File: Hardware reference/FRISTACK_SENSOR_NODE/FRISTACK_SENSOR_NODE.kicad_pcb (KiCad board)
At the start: 2 copper layers, 30 x 55 mm, 68 parts, among them J1 SPI_Header, J2 I2C/GPIO/I2S, J3 BATT, U1 ESP32-H2-MINI-1, Y1 32.768 kHz

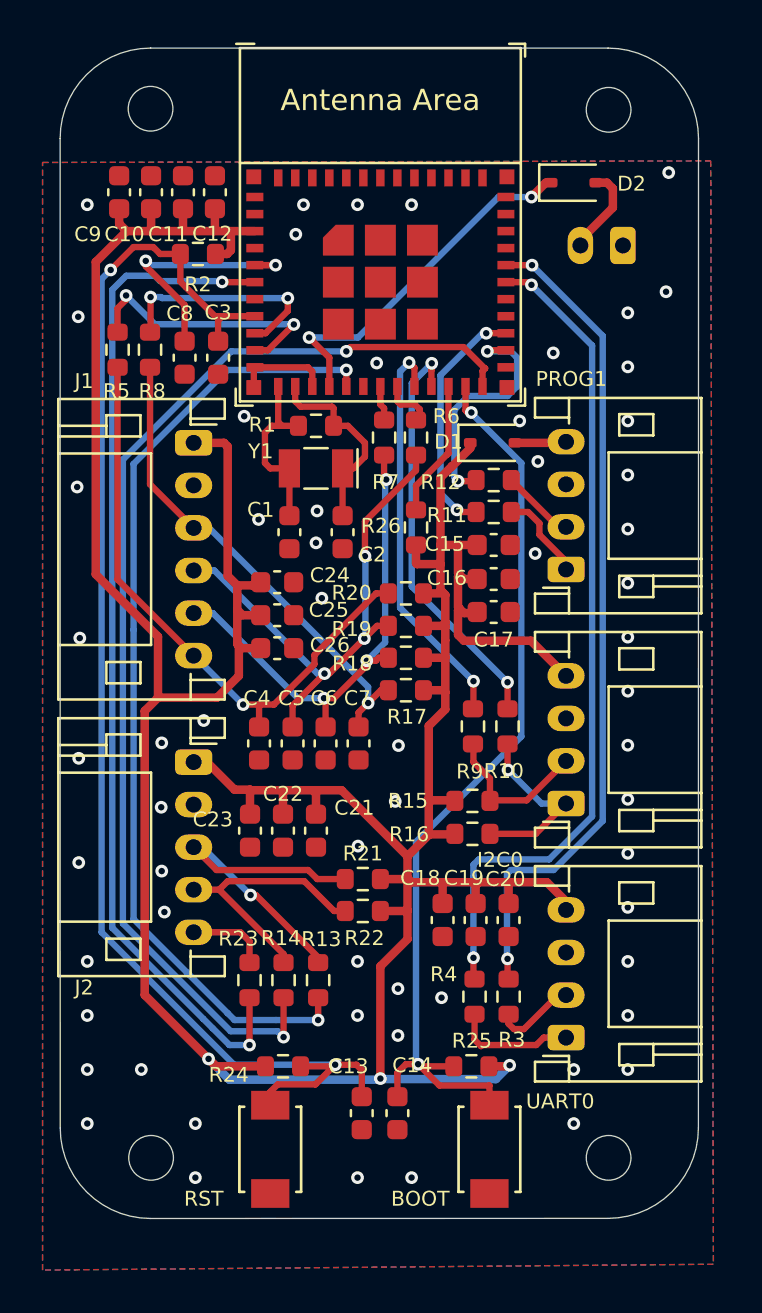
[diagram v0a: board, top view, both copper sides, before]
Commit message: Power management changes on CORE and SENSOR_NODE
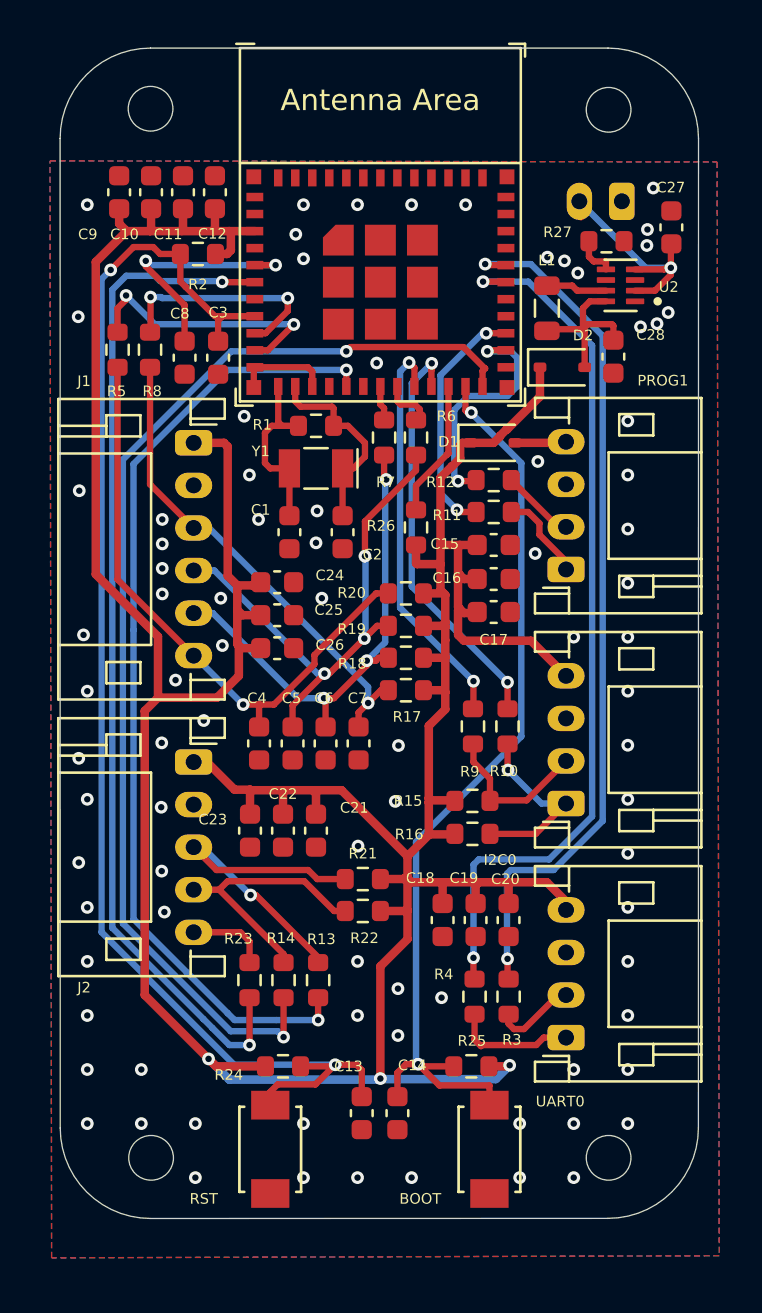
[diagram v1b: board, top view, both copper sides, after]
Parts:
- added C27: 4.7uF, Capacitor_SMD:C_0603_1608Metric, F.Cu at (188.9, 72.7)
- added C28: 10uF, Capacitor_SMD:C_0603_1608Metric, F.Cu at (186.2, 78.8)
- added L1: 2.2uH, Inductor_SMD:L_0805_2012Metric, F.Cu at (183.1, 76.5)
- added R27: 267k, Resistor_SMD:R_0603_1608Metric, F.Cu at (185.9, 73.3)
- added U2: TPS62840DLCR, User_imports:SON50P200X150X100-8N, F.Cu at (186.6, 75.4)
- moved D2 8.69 mm to (183.8, 79.2)
- moved J3 2.08 mm to (186.6, 71.5)
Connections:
- D2 pad 1: Net-(D2-K) -> ESP_PWR
- J3 pad 2: Net-(D2-A) -> VBAT
- U1 pad 15: Net-(D2-K) -> unconnected-(U1-VBAT-Pad15)
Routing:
- net Net-(D2-K): track 17.0 -> 0.00 mm, vias 2 -> 0
- net VBAT: track 0.00 -> 10.8 mm, vias 0 -> 1
- net ESP_PWR: track 177.7 -> 183.4 mm
- net Net-(D2-A): track 4.22 -> 7.59 mm
- net Net-(U2-SW): track 0.00 -> 2.87 mm
- net Net-(U1-GPIO23/FSPICS1/U0RXD): track 39.4 -> 41.6 mm
- net Net-(U2-VSET): track 0.00 -> 1.99 mm
- net Net-(U1-GPIO24/FSPICS2/U0TXD): track 39.2 -> 41.2 mm
- net GND: vias 61 -> 85

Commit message: Added logos, annotations
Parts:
- removed R13: 22, Resistor_SMD:R_0603_1608Metric
- added G***: LOGO, User_imports:fri_logo, B.Cu at (175.2, 93.7)
- added G***: LOGO, User_imports:SENsor_node_logo, B.Cu at (175.2, 75.0)
- added G***: LOGO, User_imports:lead_free, B.Cu at (185.2, 76.5)
- C27, C28: footprint Capacitor_SMD:C_0603_1608Metric -> Capacitor_SMD:C_0402_1005Metric
- L1: footprint Inductor_SMD:L_0805_2012Metric -> User_imports:INDC2016X120N
- moved R23 3.18 mm to (172.3, 108.0)
- moved L1 0.28 mm to (183.4, 76.5)
- moved C28 0.17 mm to (186.2, 78.6)
- moved C27 0.12 mm to (188.9, 72.8)
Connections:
- J2 pad 5: GPIO03 -> ADC1
- R23 pad 1: GPIO03 -> SDA1
- U1 pad 16: Net-(U1-GPIO12) -> unconnected-(U1-GPIO12-Pad16)
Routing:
- net Net-(U1-GPIO12): track 45.7 -> 0.00 mm, vias 2 -> 0
- net ADC1: track 11.7 -> 53.7 mm, vias 2 -> 3
- net GPIO03: track 4.17 -> 0.00 mm
- net CS_ESP: track 12.7 -> 11.5 mm
- net Net-(U1-GPIO3/FSPIHD/ADC1_CH2/MTDO): track 48.1 -> 49.0 mm
- net ESP_PWR: track 183.4 -> 184.3 mm
- net SDA1: track 16.0 -> 16.5 mm, vias 1 -> 2
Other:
- board text added: "ADC_1/IO2 TMS"
- board text added: "CS/IO1"
- board text added: "ESP_PWR"
- board text added: "GND"
- board text added: "MISO/IO0"
- board text added: "MOSI/IO5 TDI"
- board text added: "SCK/IO4 TCK"
- board text added: "SCL0/IO11"
- board text added: "SCL1/IO22"
- board text added: "SDA0/IO10"
- board text added: "SDA1/IO12 TDO"
- board text added: "UART0_RX"
- board text added: "UART0_TX"
- board text added: "USB_DN"
- board text added: "USB_DP"

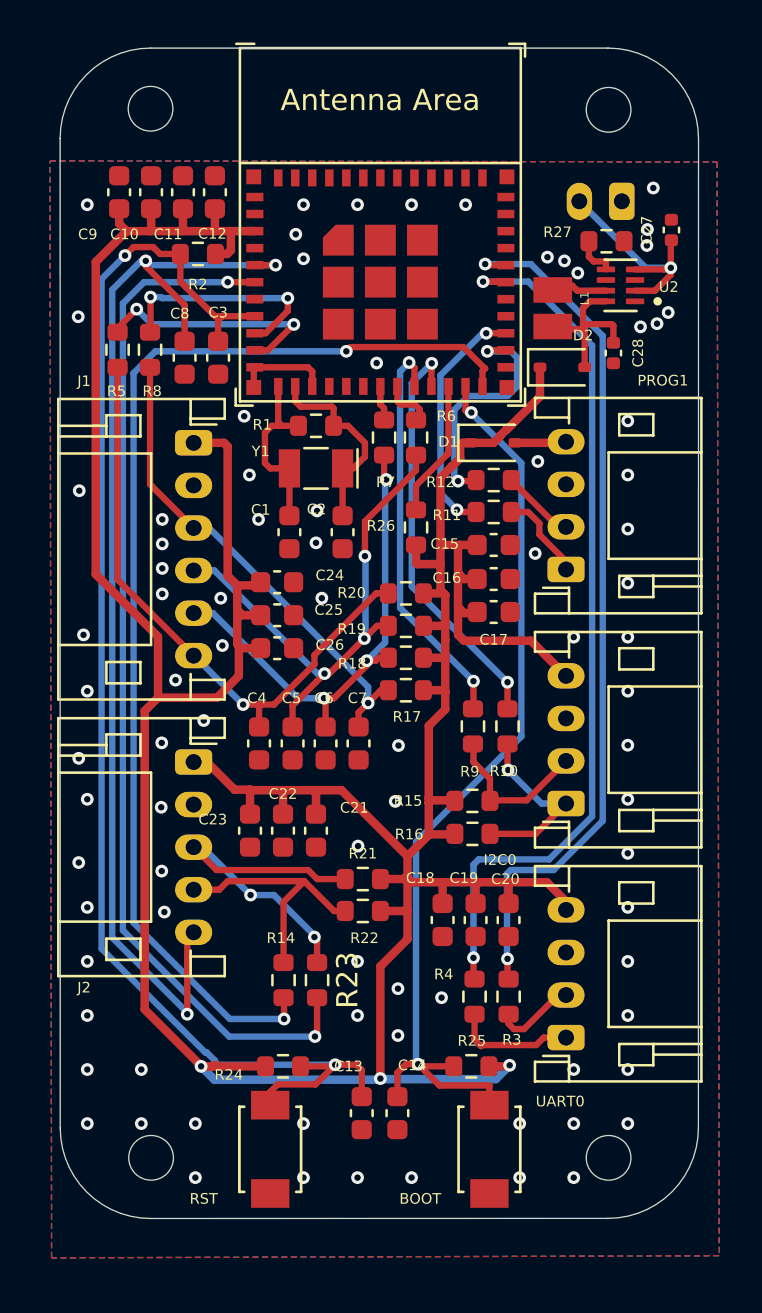
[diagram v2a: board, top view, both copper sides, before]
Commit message: review and new BATTERY board
IOT - changed twai termination from header to switch option, new holes , added power planes
SENSOR NODE - new holes and back silk text
CORE - vertical twai termination header changed to horizontal
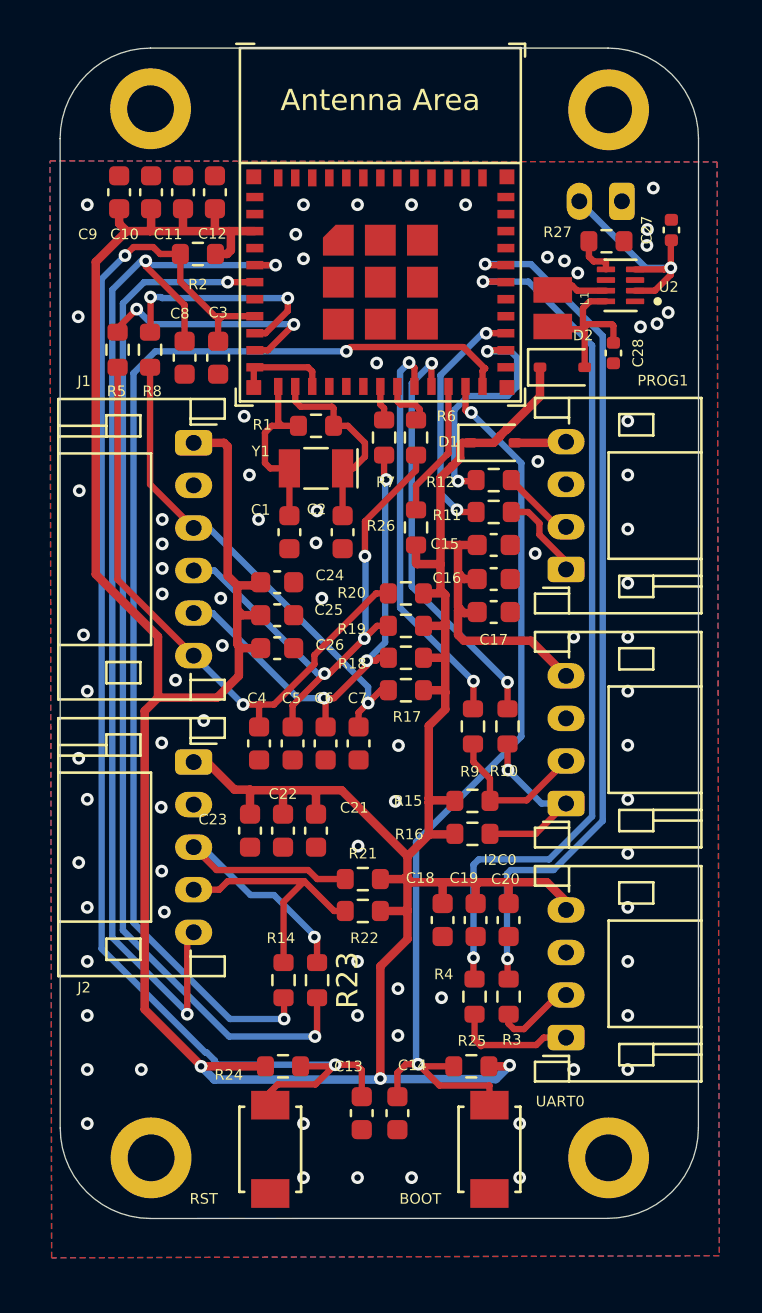
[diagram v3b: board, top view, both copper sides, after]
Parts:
- removed the G*** at (175.2, 75.0)
- removed REF** (x4): MountingHole_2.1mm, MountingHole:MountingHole_2.1mm
- added ?: , clipboard:622c10b6-db75-403c-84c1-658ef0b72b12, F.Cu at (164.5, 114.5)
- added ?: , clipboard:622c10b6-db75-403c-84c1-658ef0b72b12, F.Cu at (186.0, 114.5)
- added ?: , clipboard:622c10b6-db75-403c-84c1-658ef0b72b12, F.Cu at (164.5, 65.2)
- added ?: , clipboard:622c10b6-db75-403c-84c1-658ef0b72b12, F.Cu at (186.0, 65.2)
- added G***: LOGO, BatteryFRISTACK:sensornode, B.Cu at (175.5, 75.7)
- moved G*** 5.98 mm to (178.0, 99.0)
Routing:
- net ESP_PWR: track 184.3 -> 183.6 mm
- net SDA1: vias 2 -> 1
- net GND: vias 85 -> 79
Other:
- board text added: "Designed by Andrej Šimkovič & Marián Bobček 2025"

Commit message: Changes to Core and Sensor Node
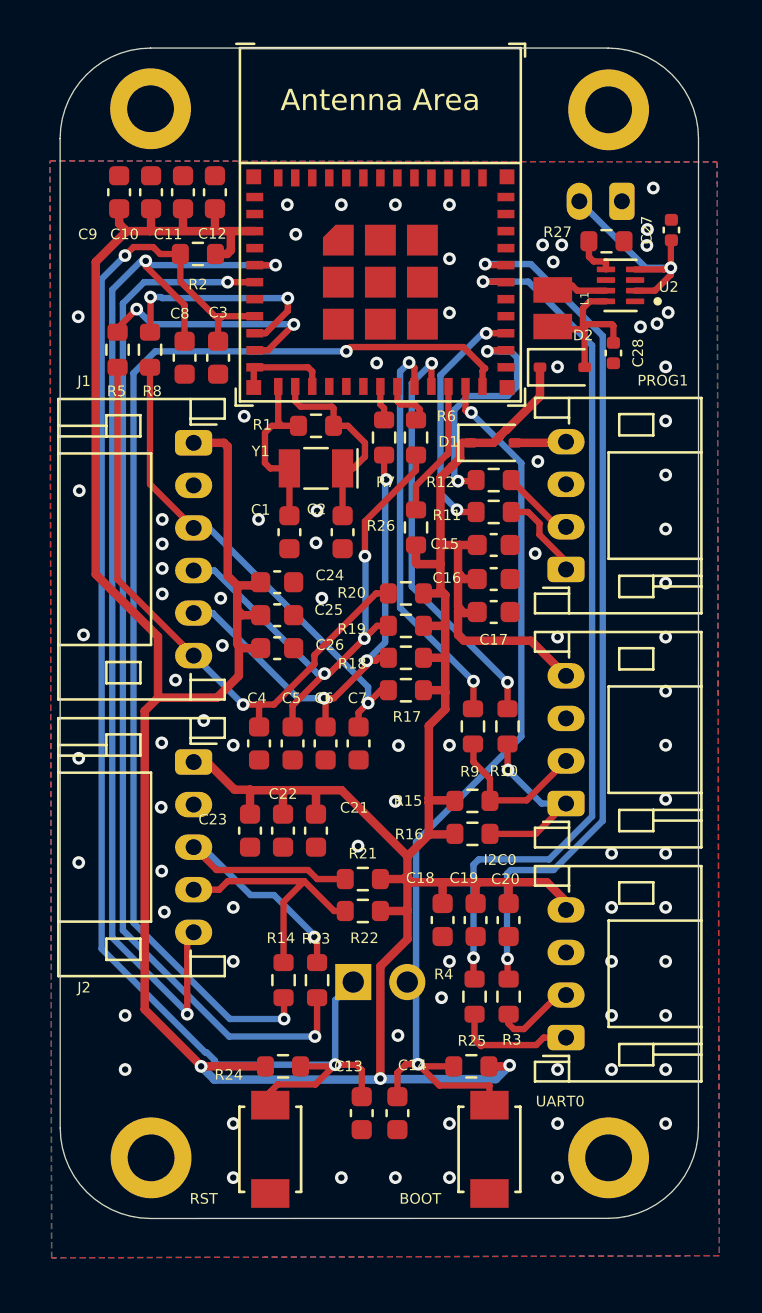
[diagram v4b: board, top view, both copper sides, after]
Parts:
- added J4: JTAG_PIN_HEADER, Connector_PinHeader_2.54mm:PinHeader_1x02_P2.54mm_Horizontal, B.Cu at (174.0, 108.1)
- moved G*** 21.0 mm to (164.2, 76.4)
- moved G*** 0.83 mm to (178.8, 99.0)
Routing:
- net EN: track 64.4 -> 68.6 mm
- net GND: vias 79 -> 84
